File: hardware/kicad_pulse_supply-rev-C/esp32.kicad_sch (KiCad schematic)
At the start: 29 parts, among them J1 USB_B_Micro, Q1 MMBT2222*, Q2 MMBT2222*, SW1 KMR211GLFS, U1 AP2112K-3.3, U2 ESP32-WROOM-32D, U3 CP2104

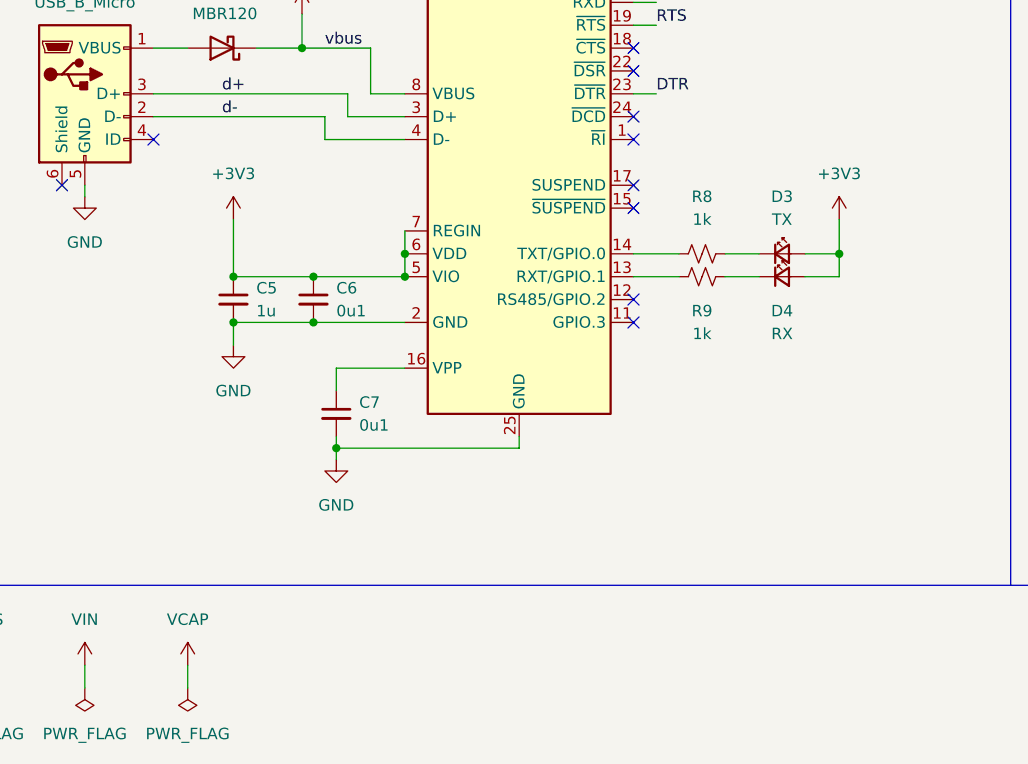
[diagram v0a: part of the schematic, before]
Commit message: Refactored main loop to use Arduino Strings
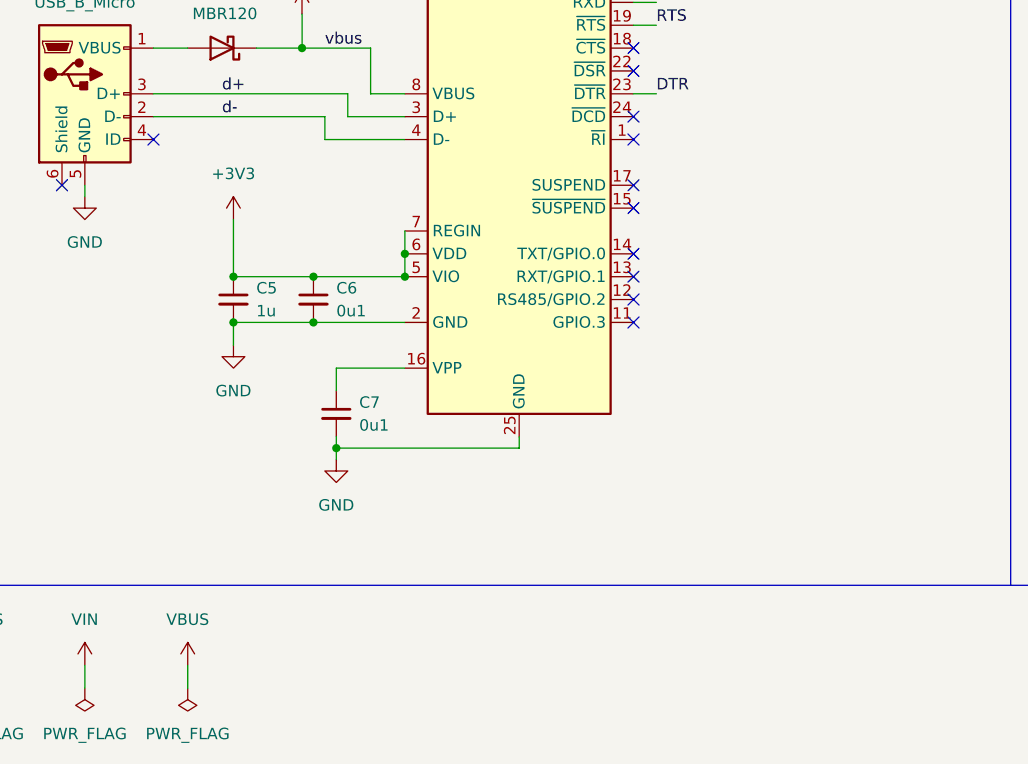
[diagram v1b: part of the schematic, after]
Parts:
- removed D3: TX, LED_SMD:LED_0603_1608Metric_Pad1.05x0.95mm_HandSolder, symbol Device:LED_Small
- removed D4: RX, LED_SMD:LED_0603_1608Metric_Pad1.05x0.95mm_HandSolder, symbol Device:LED_Small
- removed R8, R9: 1k, Resistor_SMD:R_0603_1608Metric_Pad0.98x0.95mm_HandSolder, symbol Device:R_Small_US
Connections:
- no-connect marks 31 -> 33

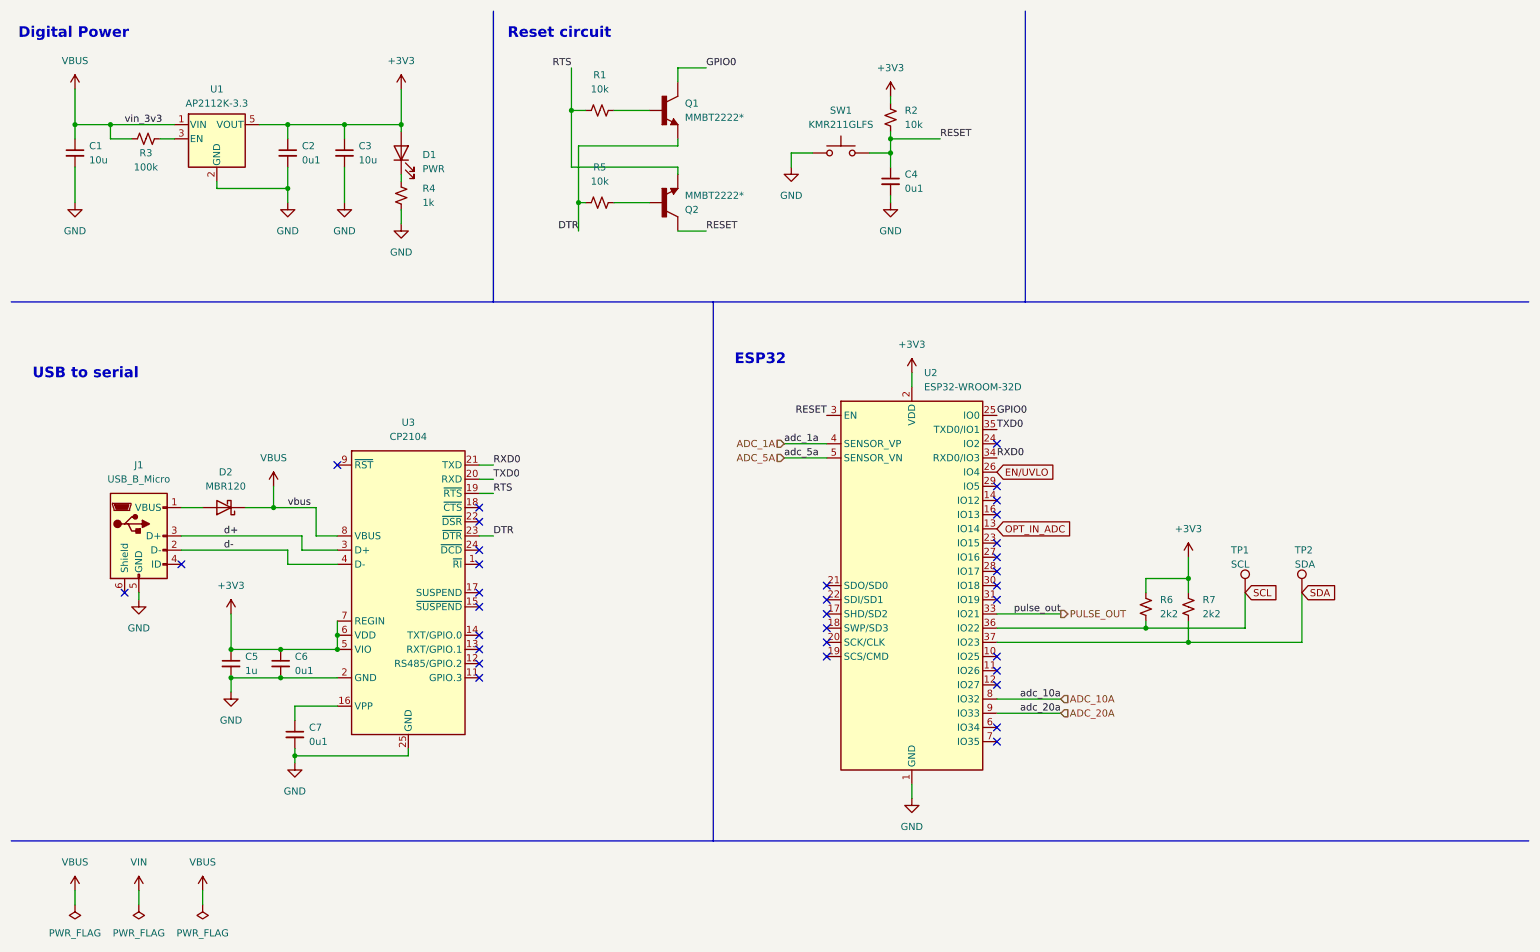
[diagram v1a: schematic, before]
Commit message: hardware breakout boards added, pcb rev-c began
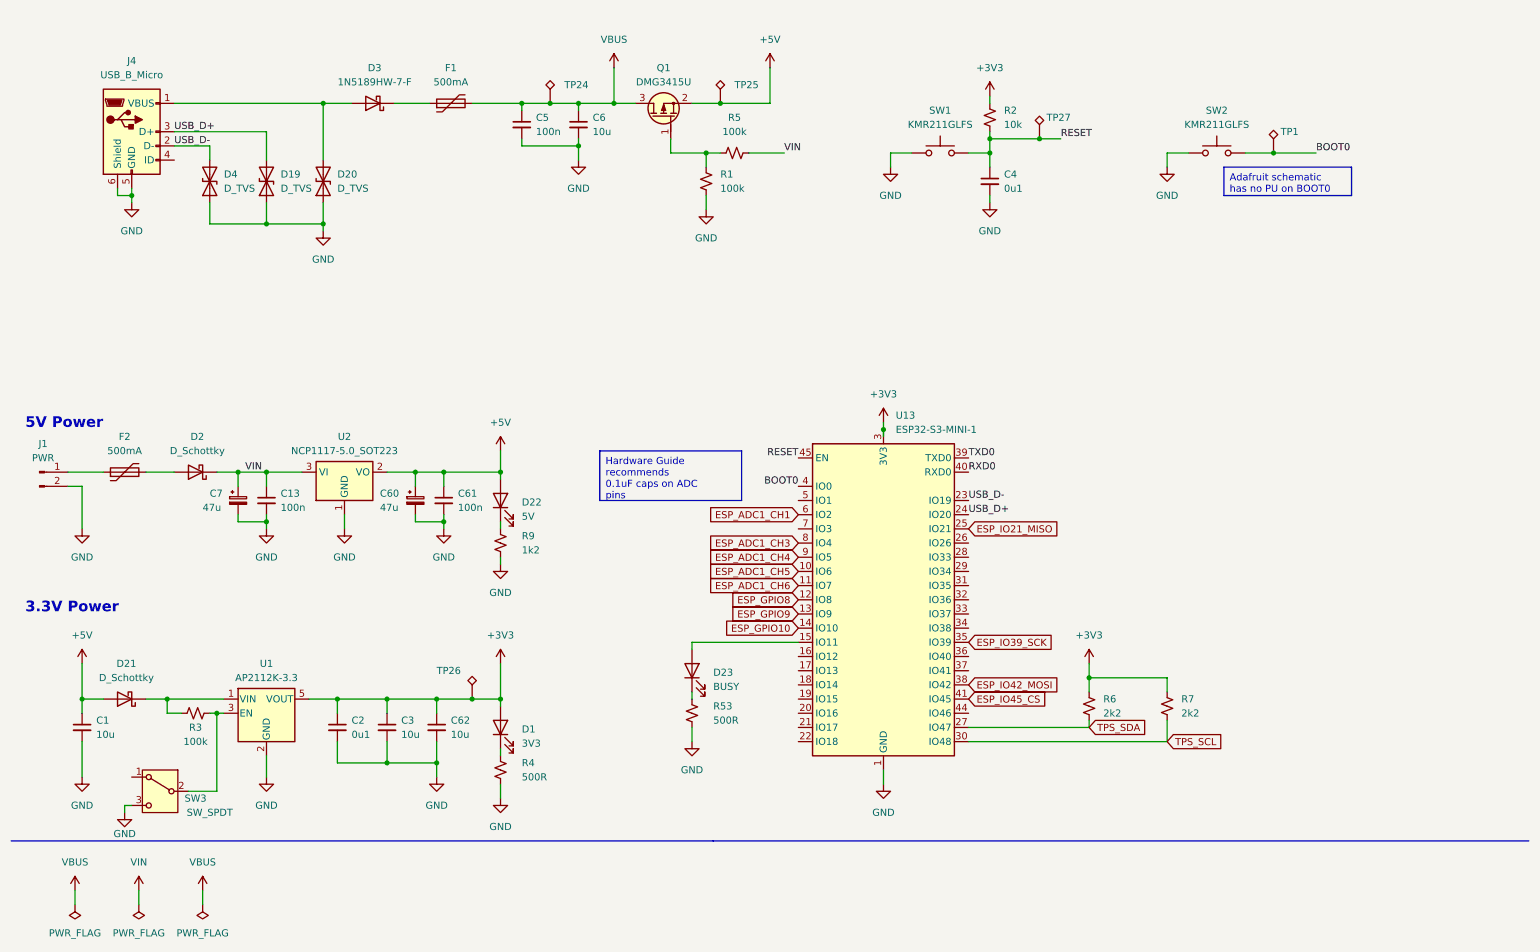
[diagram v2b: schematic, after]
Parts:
- removed C7: 0u1, Capacitor_SMD:C_0603_1608Metric_Pad1.08x0.95mm_HandSolder, symbol Device:C_Small
- removed J1: USB_B_Micro, DW_Library:USB_Micro-B_Amphenol_10118194_Horizontal, symbol Connector:USB_B_Micro
- removed Q1, Q2: MMBT2222*, Package_TO_SOT_SMD:SOT-23, symbol DW_custom_symbols:MMBT2222*
- removed TP1: SCL, DW_Library:Keystone-1502-2, symbol Connector:TestPoint
- removed TP2: SDA, DW_Library:Keystone-1502-2, symbol Connector:TestPoint
- removed U2: ESP32-WROOM-32D, RF_Module:ESP32-WROOM-32D, symbol RF_Module:ESP32-WROOM-32D
- removed U3: CP2104, Package_DFN_QFN:QFN-24-1EP_4x4mm_P0.5mm_EP2.6x2.6mm, symbol DW_custom_symbols:CP2104
- added C13, C61: 100n, symbol Device:C_Small
- added C60, C7: 47u, symbol Device:C_Polarized_Small
- added C62: 10u, Capacitor_SMD:C_0805_2012Metric_Pad1.18x1.45mm_HandSolder, symbol Device:C_Small
- added D19, D20, D4: D_TVS, symbol Device:D_TVS
- added D21: D_Schottky, symbol Device:D_Schottky
- added D22: 5V, LED_SMD:LED_0603_1608Metric_Pad1.05x0.95mm_HandSolder, symbol Device:LED
- added D23: BUSY, LED_SMD:LED_0603_1608Metric_Pad1.05x0.95mm_HandSolder, symbol Device:LED
- added D3: 1N5189HW-7-F, symbol Device:D_Schottky
- added F1, F2: 500mA, symbol Device:Polyfuse
- added J1: PWR, symbol Connector:Conn_01x02_Pin
- added J4: USB_B_Micro, symbol Connector:USB_B_Micro
- added Q1: DMG3415U, PCM_Package_TO_SOT_SMD_AKL:SOT-23, symbol PCM_Transistor_MOSFET_AKL:DMG3415U
- added R53: 500R, Resistor_SMD:R_0603_1608Metric_Pad0.98x0.95mm_HandSolder, symbol Device:R_Small_US
- added R9: 1k2, Resistor_SMD:R_0603_1608Metric_Pad0.98x0.95mm_HandSolder, symbol Device:R_Small_US
- added SW2: KMR211GLFS, Button_Switch_SMD:SW_Push_1P1T-SH_NO_CK_KMR2xxG, symbol Switch:SW_Push
- added SW3: SW_SPDT, symbol Switch:SW_SPDT
- added TP1, TP24, TP25, TP26, TP27: ~, symbol Connector:TestPoint_Alt
- added U13: ESP32-S3-MINI-1, RF_Module:ESP32-S2-MINI-1, symbol MCU_Espressif:ESP32-S3-MINI-1
- added U2: NCP1117-5.0_SOT223, Package_TO_SOT_SMD:SOT-223-3_TabPin2, symbol Regulator_Linear:NCP1117-5.0_SOT223
- C5: value 1u -> 100n; footprint Capacitor_SMD:C_0603_1608Metric_Pad1.08x0.95mm_HandSolder -> (none)
- C6: value 0u1 -> 10u; footprint Capacitor_SMD:C_0603_1608Metric_Pad1.08x0.95mm_HandSolder -> (none)
- D1: value PWR -> 3V3
- D2: value MBR120 -> D_Schottky; footprint Diode_SMD:D_SOD-123F -> (none)
- R1, R5: value 10k -> 100k; footprint Resistor_SMD:R_0603_1608Metric_Pad0.98x0.95mm_HandSolder -> (none)
- R4: value 1k -> 500R
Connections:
- net RTS is gone; now on an unnamed net: R1.1
- net +3V3: now also C62.1, TP26.1, U13.3 (3V3); no longer C5.1, C6.1
- net GND: now also R1.2, C13.2, C60.2, C61.2, C62.2, C7.2, D19.1 (A1), D20.1 (A1), D4.1 (A1), J1.2 (Pin_2), J4.5 (GND), J4.6 (Shield), R53.1, R9.1, SW2.1, SW3.3 (C), U13.1 (GND), U13.2 (GND), U13.42 (GND), U13.43 (GND), U13.46 (GND), U13.47 (GND), U13.48 (GND), U13.49 (GND), U13.50 (GND), U13.51 (GND), U13.52 (GND), U13.53 (GND), U13.54 (GND), U13.55 (GND), U13.56 (GND), U13.57 (GND), U13.58 (GND), U13.59 (GND), U13.60 (GND), U13.61 (GND), U13.62 (GND), U13.63 (GND), U13.64 (GND), U13.65 (GND), U2.1 (GND)
- net RESET: now also TP27.1, U13.45 (EN)
- net RXD0: now also U13.40 (RXD0)
- net TXD0: now also U13.39 (TXD0)
- net VBUS: now also C5.1, C6.1, F1.2, Q1.3 (D), TP24.1; no longer C1.1, D2.1 (K), R3.1, U1.1 (VIN)
- net VIN: now also D2.1 (K), R5.2, C13.1, C7.1, U2.3 (VI)
- net at D2.2 (A): now also F2.2
- net at R3.2, U1.3 (EN): now also SW3.2 (B)
- net DTR: no longer names the net of R5.1
- net DTR: now also Q1.1 (G)
- net SCL renamed TPS_SDA
- net TPS_SDA: now also U13.27 (IO47)
- net SDA renamed TPS_SCL
- net TPS_SCL: now also U13.30 (IO48)
- new net: F2.1, J1.1 (Pin_1)
- new net: D3.1 (K), F1.1
- new net: D20.2 (A2), D3.2 (A), J4.1 (VBUS)
- new net: D22.1 (K), R9.2
- new net: D21.1 (K), R3.1, U1.1 (VIN)
- new net: D23.1 (K), R53.2
- new net: D23.2 (A), U13.15 (IO11)
- new net +5V: C1.1, C60.1, C61.1, D21.2 (A), D22.2 (A), Q1.2 (S), TP25.1, U2.2 (VO)
- new net BOOT0: SW2.2, TP1.1, U13.4 (IO0)
- new net ESP_ADC1_CH1: U13.6 (IO2)
- new net ESP_ADC1_CH3: U13.8 (IO4)
- new net ESP_ADC1_CH4: U13.9 (IO5)
- new net ESP_ADC1_CH5: U13.10 (IO6)
- new net ESP_ADC1_CH6: U13.11 (IO7)
- new net ESP_GPIO10: U13.14 (IO10)
- new net ESP_GPIO8: U13.12 (IO8)
- new net ESP_GPIO9: U13.13 (IO9)
- new net ESP_IO21_MISO: U13.25 (IO21)
- new net ESP_IO39_SCK: U13.35 (IO39)
- new net ESP_IO42_MOSI: U13.38 (IO42)
- new net ESP_IO45_CS: U13.41 (IO45)
- new net USB_D+: D19.2 (A2), J4.3 (D+), U13.24 (IO20)
- new net USB_D-: D4.2 (A2), J4.2 (D-), U13.23 (IO19)
- no-connect marks 33 -> 0
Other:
- note added: "3.3V Power"
- note added: "5V Power"
- note removed: "Digital Power"
- note removed: "ESP32"
- note removed: "Reset circuit"
- note removed: "USB to serial"
- moved on the sheet: C1, C2, C3, C4, D1, R2, R3, R4, R6, R7, SW1, U1
